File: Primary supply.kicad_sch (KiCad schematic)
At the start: 55 parts, among them K301 RZ03-1A4-D012, Q301 BC807, Q302 BC817, Q303 BC817

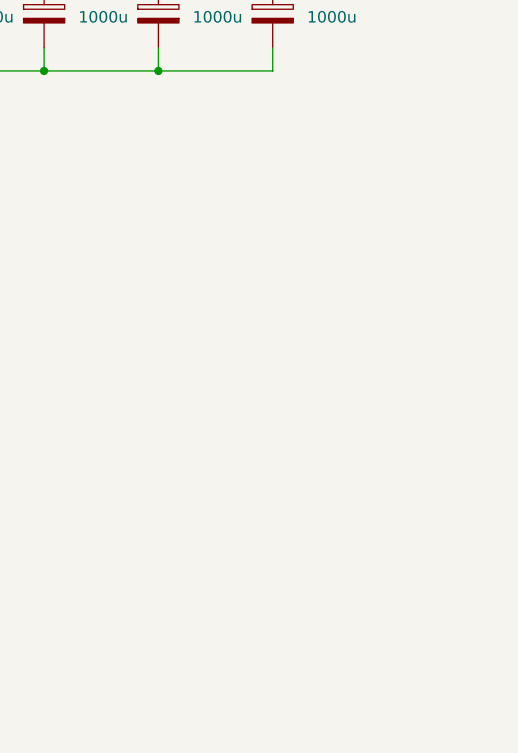
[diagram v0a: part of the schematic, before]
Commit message: Add connection testpoints and noise reduction capacitors
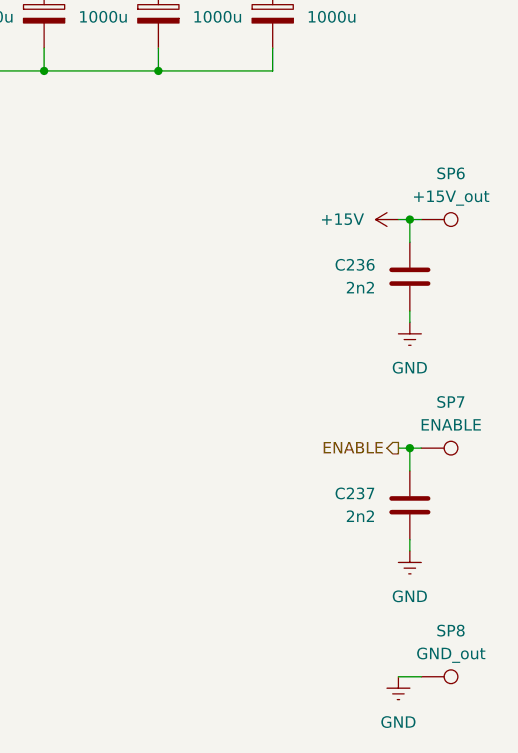
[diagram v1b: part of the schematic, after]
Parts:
- added C236, C237: 2n2, symbol Device:C
- added SP6: +15V_out, symbol Connector:TestPoint
- added SP7: ENABLE, symbol Connector:TestPoint
- added SP8: GND_out, symbol Connector:TestPoint
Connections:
- net +15V: now also C236.1, SP6.1
- net ENABLE: now also C237.1, SP7.1
- net GND: now also C236.2, C237.2, SP8.1

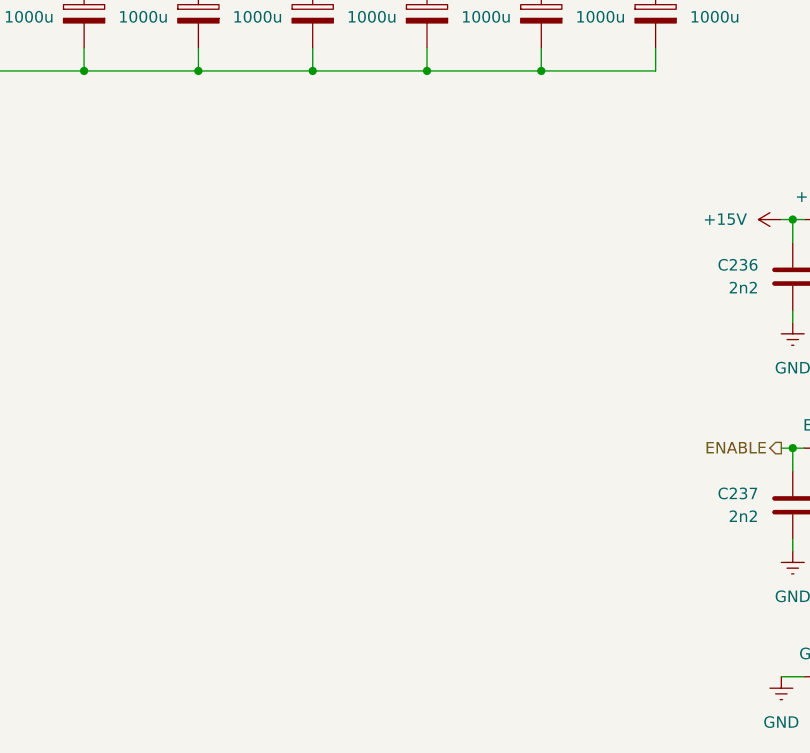
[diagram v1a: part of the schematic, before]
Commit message: Separate 3.3V 1A pwm output stage to another sheet
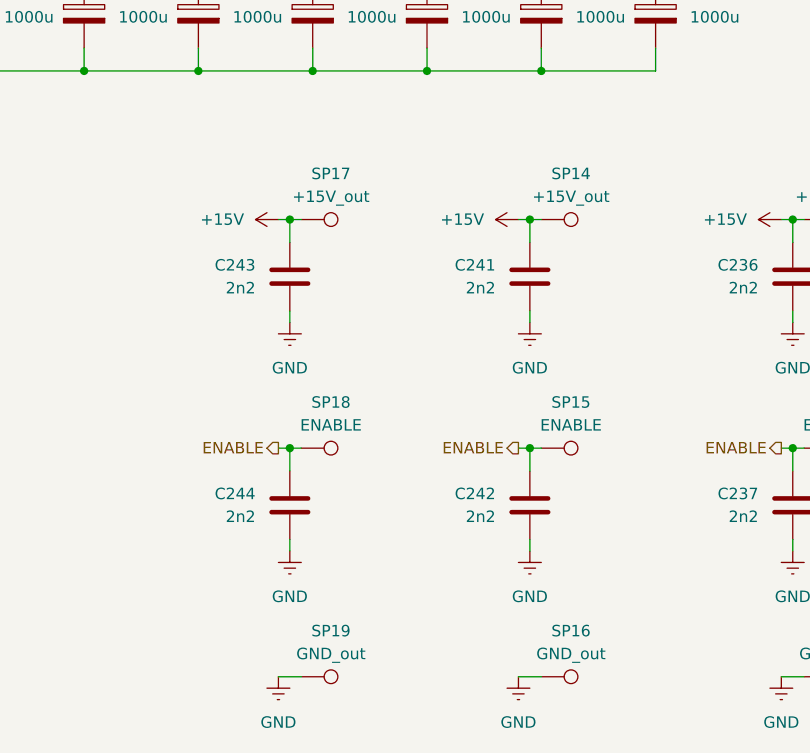
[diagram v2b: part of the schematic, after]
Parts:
- added C241, C242, C243, C244: 2n2, symbol Device:C
- added SP14, SP17: +15V_out, symbol Connector:TestPoint
- added SP15, SP18: ENABLE, symbol Connector:TestPoint
- added SP16, SP19: GND_out, symbol Connector:TestPoint
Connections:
- net +15V: now also C241.1, C243.1, SP14.1, SP17.1
- net ENABLE: now also C242.1, C244.1, SP15.1, SP18.1
- net GND: now also C241.2, C242.2, C243.2, C244.2, SP16.1, SP19.1

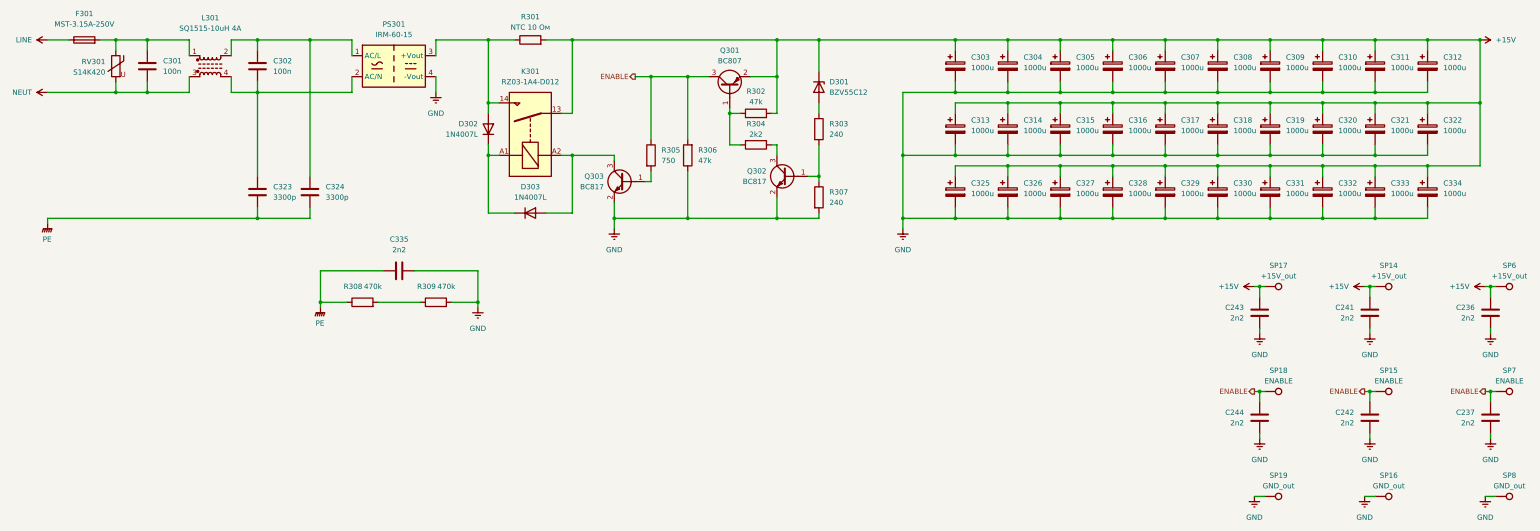
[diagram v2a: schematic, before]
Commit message: Add FX30B-5S-3.81DSA connector library files
- Created a new symbol file for the FX30B-5S-3.81DSA connector in Muon_Library.kicad_sym.
- Added a new footprint for the FX30B-5S-3.81DSA connector in Muon_Library.pretty/FX30B-5S-3.81DSA.kicad_mod.
- Included a PDF datasheet for the connector in the library.
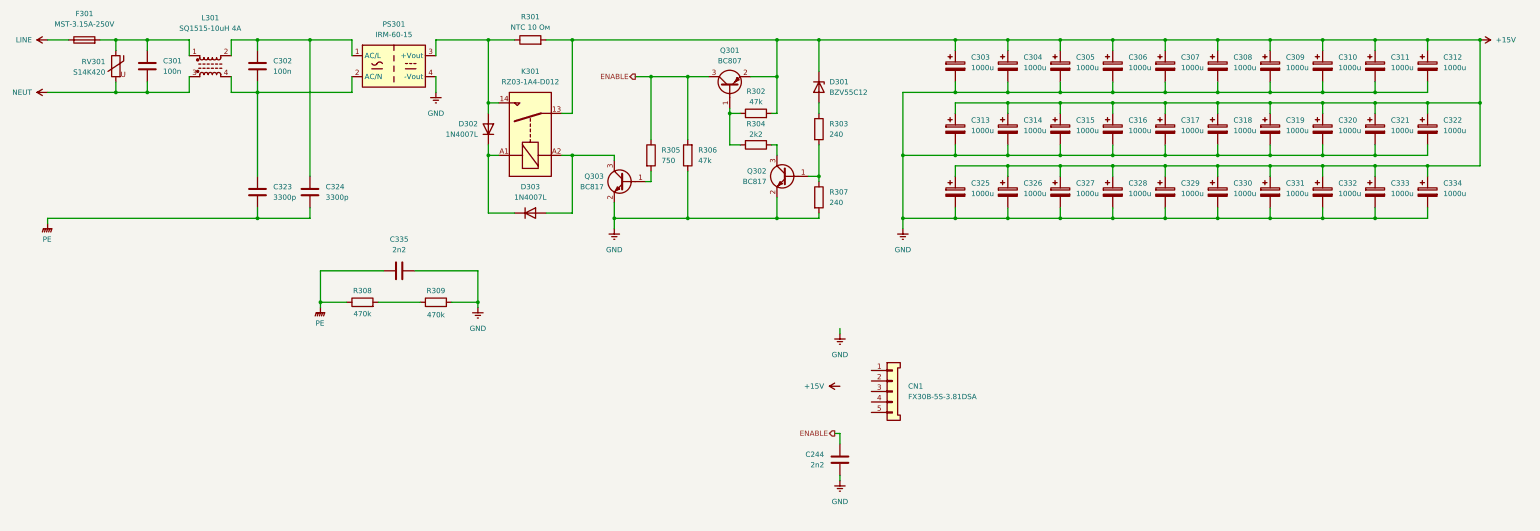
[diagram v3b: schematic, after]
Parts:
- removed C236, C237, C241, C242, C243: 2n2, symbol Device:C
- removed SP14, SP17, SP6: +15V_out, symbol Connector:TestPoint
- removed SP15, SP18, SP7: ENABLE, symbol Connector:TestPoint
- removed SP16, SP19, SP8: GND_out, symbol Connector:TestPoint
- added CN1: FX30B-5S-3.81DSA, Muon_Library:FX30B-5S-3.81DSA, symbol Muon_Library:FX30B-5S-3.81DSA
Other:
- moved on the sheet: C244
